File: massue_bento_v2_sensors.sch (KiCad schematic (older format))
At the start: 0 parts

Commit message: Merge branch 'master' of https://github.com/tommag/massue_bento_v2
Conflicts:
	massue_bento_v2_power.sch
	massue_bento_v2_rf.sch
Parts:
- added C?: 10nF, symbol C
- added C? (x2): 0.1uF, symbol C
- added C?: 2.2nF, symbol C
- added C?: 100nF, symbol C
- added U?: MPU9150, symbol MPU9150
- added U?: MS5607, symbol MS5607
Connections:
- new net: C?.1, U?.10 (REGOUT)
- new net: C?.2, U?.20 (CPOUT)
- new net +3.3V: C?.1, C?.1, C?.1, U?.1 (VDD), U?.13 (VDD), U?.2 (PS), U?.3 (VDD), U?.8 (VLOGIC)
- new net GND: C?.1, C?.2, C?.2, C?.2, C?.2, U?.1 (CLKIN), U?.11 (FSYNC), U?.15 (GND), U?.17 (GND), U?.18 (GND), U?.3 (GND), U?.4 (CSB), U?.5 (CSB), U?.9 (AD0)
- new net MPU9150_INT: U?.12 (INT)
- new net SCL: U?.23 (SCL), U?.8 (SCLK)
- new net SDA: U?.24 (SDA), U?.7 (SDI/SDA)
- no-connect marks 0 -> 3

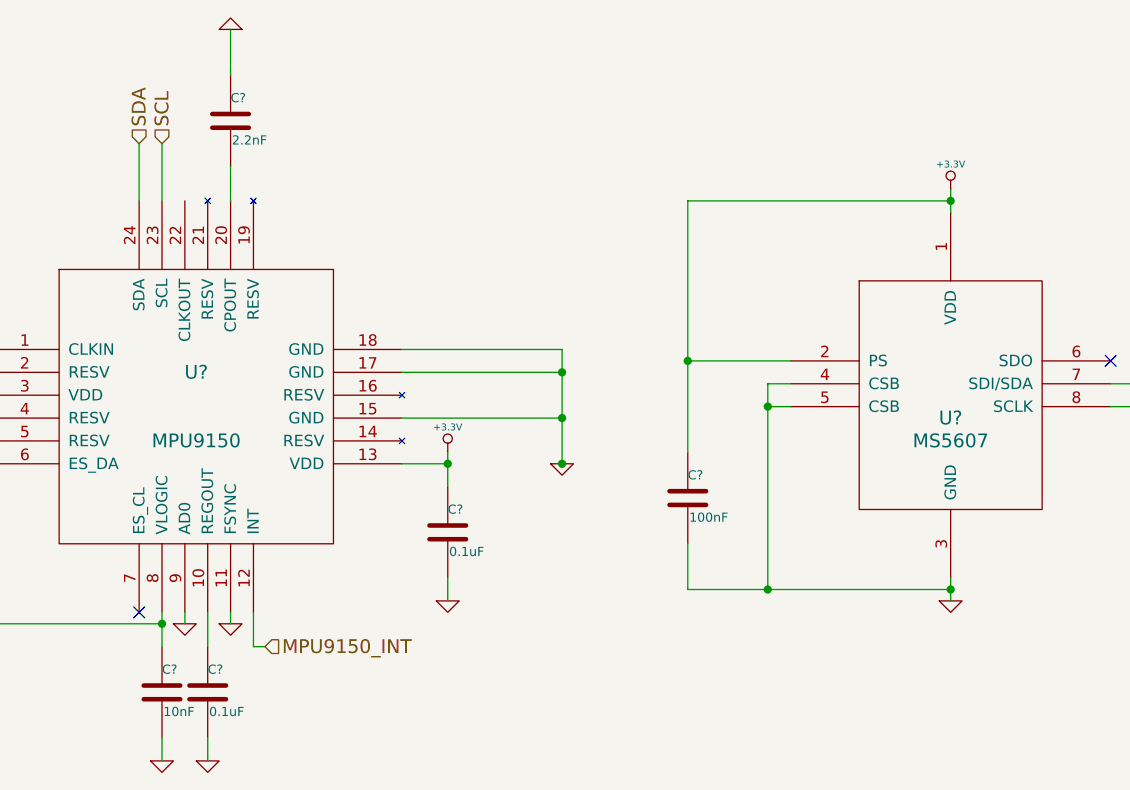
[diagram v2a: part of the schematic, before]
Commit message: Fix: global annotation, fixed bugs to satisfy ERC
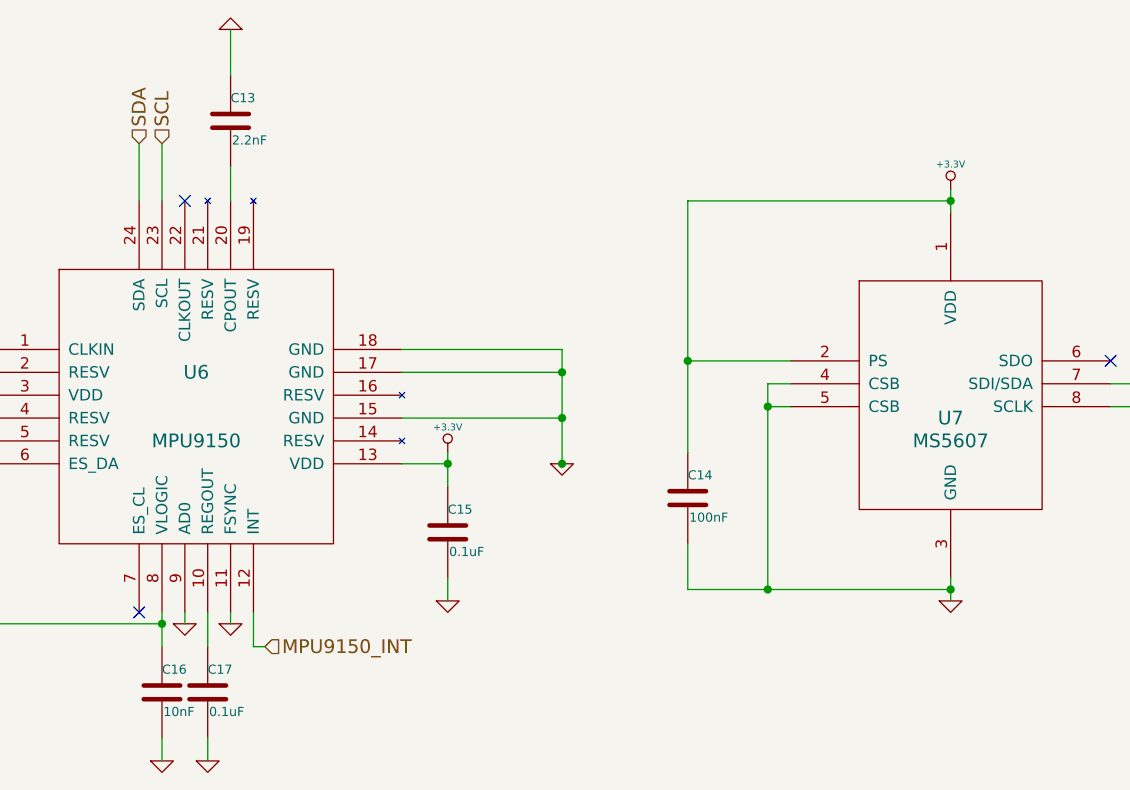
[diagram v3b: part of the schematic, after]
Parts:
- gave numbers to parts that had none: 7
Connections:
- no-connect marks 3 -> 4
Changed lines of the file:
@@
 $EndDescr
 $Comp
-L MPU9150 U?
+L MPU9150 U6
 U 1 1 53A574BD
 P 5700 4250
-F 0 "U?" H 5700 4400 60  0000 C CNN
+F 0 "U6" H 5700 4400 60  0000 C CNN
 F 1 "MPU9150" H 5700 4100 60  0000 C CNN
 F 2 "" H 5700 4250 60  0000 C CNN
@@
 SCL
 $Comp
-L GND #PWR?
+L GND #PWR057
 U 1 1 53A57668
 P 7300 4500
-F 0 "#PWR?" H 7300 4500 30  0001 C CNN
+F 0 "#PWR057" H 7300 4500 30  0001 C CNN
 F 1 "GND" H 7300 4430 30  0001 C CNN
 F 2 "" H 7300 4500 60  0000 C CNN
@@
 $EndComp
 $Comp
-L +3.3V #PWR?
+L +3.3V #PWR058
 U 1 1 53A57758
 P 6800 4450
-F 0 "#PWR?" H 6800 4410 30  0001 C CNN
+F 0 "#PWR058" H 6800 4410 30  0001 C CNN
 F 1 "+3.3V" H 6800 4560 30  0000 C CNN
 F 2 "" H 6800 4450 60  0000 C CNN
@@
 $EndComp
 $Comp
-L +3.3V #PWR?
+L +3.3V #PWR059
 U 1 1 53A57777
 P 4300 4200
-F 0 "#PWR?" H 4300 4160 30  0001 C CNN
+F 0 "#PWR059" H 4300 4160 30  0001 C CNN
 F 1 "+3.3V" H 4300 4310 30  0000 C CNN
 F 2 "" H 4300 4200 60  0000 C CNN
@@
 $EndComp
 $Comp
-L C C?
+L C C16
 U 1 1 53A57917
 P 5550 5500
-F 0 "C?" H 5550 5600 40  0000 L CNN
+F 0 "C16" H 5550 5600 40  0000 L CNN
 F 1 "10nF" H 5556 5415 40  0000 L CNN
 F 2 "" H 5588 5350 30  0000 C CNN
@@
 $EndComp
 $Comp
-L GND #PWR?
+L GND #PWR060
 U 1 1 53A57951
 P 5550 5800
-F 0 "#PWR?" H 5550 5800 30  0001 C CNN
+F 0 "#PWR060" H 5550 5800 30  0001 C CNN
 F 1 "GND" H 5550 5730 30  0001 C CNN
 F 2 "" H 5550 5800 60  0000 C CNN
@@
 $EndComp
 $Comp
-L C C?
+L C C15
 U 1 1 53A57996
 P 6800 4800
-F 0 "C?" H 6800 4900 40  0000 L CNN
+F 0 "C15" H 6800 4900 40  0000 L CNN
 F 1 "0.1uF" H 6806 4715 40  0000 L CNN
 F 2 "" H 6838 4650 30  0000 C CNN
@@
 $EndComp
 $Comp
-L GND #PWR?
+L GND #PWR061
 U 1 1 53A579C7
 P 6800 5100
-F 0 "#PWR?" H 6800 5100 30  0001 C CNN
+F 0 "#PWR061" H 6800 5100 30  0001 C CNN
 F 1 "GND" H 6800 5030 30  0001 C CNN
 F 2 "" H 6800 5100 60  0000 C CNN
@@
 $EndComp
 $Comp
-L C C?
+L C C17
 U 1 1 53A579EC
 P 5750 5500
-F 0 "C?" H 5750 5600 40  0000 L CNN
+F 0 "C17" H 5750 5600 40  0000 L CNN
 F 1 "0.1uF" H 5756 5415 40  0000 L CNN
 F 2 "" H 5788 5350 30  0000 C CNN
@@
 $EndComp
 $Comp
-L GND #PWR?
+L GND #PWR062
 U 1 1 53A57A0C
 P 5750 5800
-F 0 "#PWR?" H 5750 5800 30  0001 C CNN
+F 0 "#PWR062" H 5750 5800 30  0001 C CNN
 F 1 "GND" H 5750 5730 30  0001 C CNN
 F 2 "" H 5750 5800 60  0000 C CNN
@@
 NoConn ~ 5450 5150
 $Comp
-L GND #PWR?
+L GND #PWR063
 U 1 1 53A57AC0
 P 5650 5200
-F 0 "#PWR?" H 5650 5200 30  0001 C CNN
+F 0 "#PWR063" H 5650 5200 30  0001 C CNN
 F 1 "GND" H 5650 5130 30  0001 C CNN
 F 2 "" H 5650 5200 60  0000 C CNN
@@
 $EndComp
 $Comp
-L GND #PWR?
+L GND #PWR064
 U 1 1 53A57AE9
 P 5850 5200
-F 0 "#PWR?" H 5850 5200 30  0001 C CNN
+F 0 "#PWR064" H 5850 5200 30  0001 C CNN
 F 1 "GND" H 5850 5130 30  0001 C CNN
 F 2 "" H 5850 5200 60  0000 C CNN
@@
 MPU9150_INT
 $Comp
-L GND #PWR?
+L GND #PWR065
 U 1 1 53A57B2B
 P 4650 4050
-F 0 "#PWR?" H 4650 4050 30  0001 C CNN
+F 0 "#PWR065" H 4650 4050 30  0001 C CNN
 F 1 "GND" H 4650 3980 30  0001 C CNN
 F 2 "" H 4650 4050 60  0000 C CNN
@@
 $EndComp
 $Comp
-L C C?
+L C C13
 U 1 1 53A57B7E
 P 5850 3000
-F 0 "C?" H 5850 3100 40  0000 L CNN
+F 0 "C13" H 5850 3100 40  0000 L CNN
 F 1 "2.2nF" H 5856 2915 40  0000 L CNN
 F 2 "" H 5888 2850 30  0000 C CNN
@@
 $EndComp
 $Comp
-L GND #PWR?
+L GND #PWR066
 U 1 1 53A57BB8
 P 5850 2600
-F 0 "#PWR?" H 5850 2600 30  0001 C CNN
+F 0 "#PWR066" H 5850 2600 30  0001 C CNN
 F 1 "GND" H 5850 2530 30  0001 C CNN
 F 2 "" H 5850 2600 60  0000 C CNN
@@
 $EndComp
 $Comp
-L MS5607 U?
+L MS5607 U7
 U 1 1 53A587E2
 P 9000 4300
-F 0 "U?" H 9000 4300 60  0000 C CNN
+F 0 "U7" H 9000 4300 60  0000 C CNN
 F 1 "MS5607" H 9000 4200 60  0000 C CNN
 F 2 "" H 9000 4300 60  0000 C CNN
@@
 $EndComp
 $Comp
-L GND #PWR?
+L GND #PWR067
 U 1 1 53A587F6
 P 9000 5100
-F 0 "#PWR?" H 9000 5100 30  0001 C CNN
+F 0 "#PWR067" H 9000 5100 30  0001 C CNN
 F 1 "GND" H 9000 5030 30  0001 C CNN
 F 2 "" H 9000 5100 60  0000 C CNN
@@
 $EndComp
 $Comp
-L +3.3V #PWR?
+L +3.3V #PWR068
 U 1 1 53A58808
 P 9000 3300
-F 0 "#PWR?" H 9000 3260 30  0001 C CNN
+F 0 "#PWR068" H 9000 3260 30  0001 C CNN
 F 1 "+3.3V" H 9000 3410 30  0000 C CNN
 F 2 "" H 9000 3300 60  0000 C CNN
@@
 $EndComp
 $Comp
-L C C?
+L C C14
 U 1 1 53A58856
 P 7850 4650
-F 0 "C?" H 7850 4750 40  0000 L CNN
+F 0 "C14" H 7850 4750 40  0000 L CNN
 F 1 "100nF" H 7856 4565 40  0000 L CNN
 F 2 "" H 7888 4500 30  0000 C CNN
@@
 	9700 4250 9850 4250
 NoConn ~ 9700 4050
+NoConn ~ 5650 3350
 $EndSCHEMATC

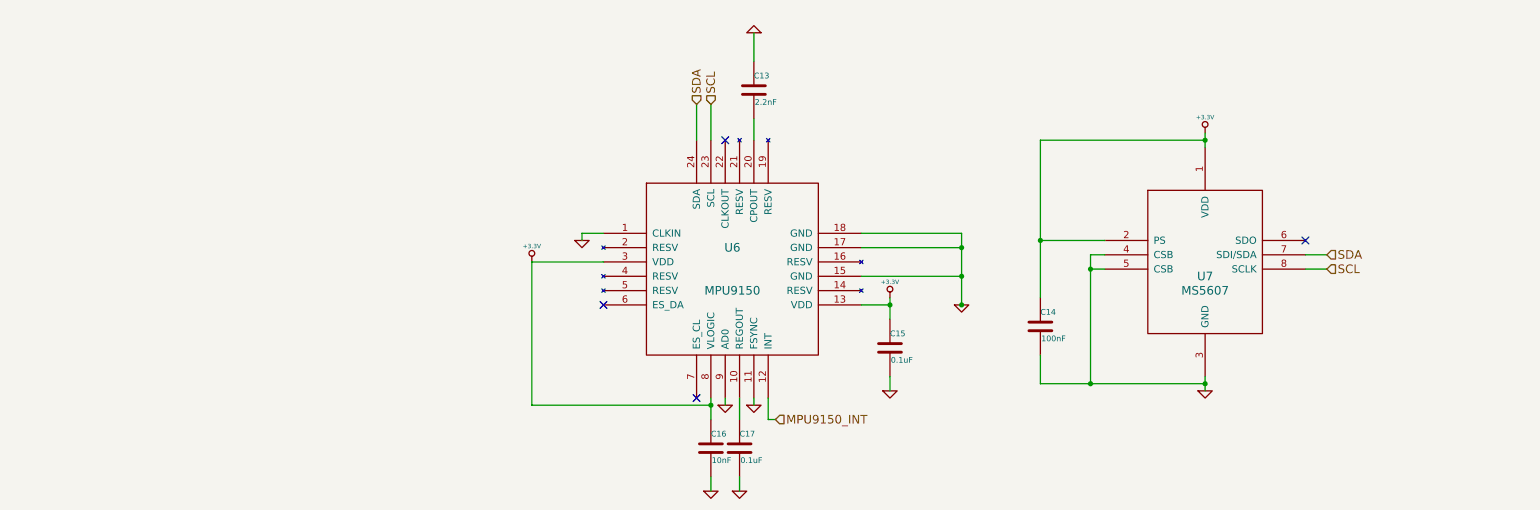
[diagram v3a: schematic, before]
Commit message: New : AT42 sensor
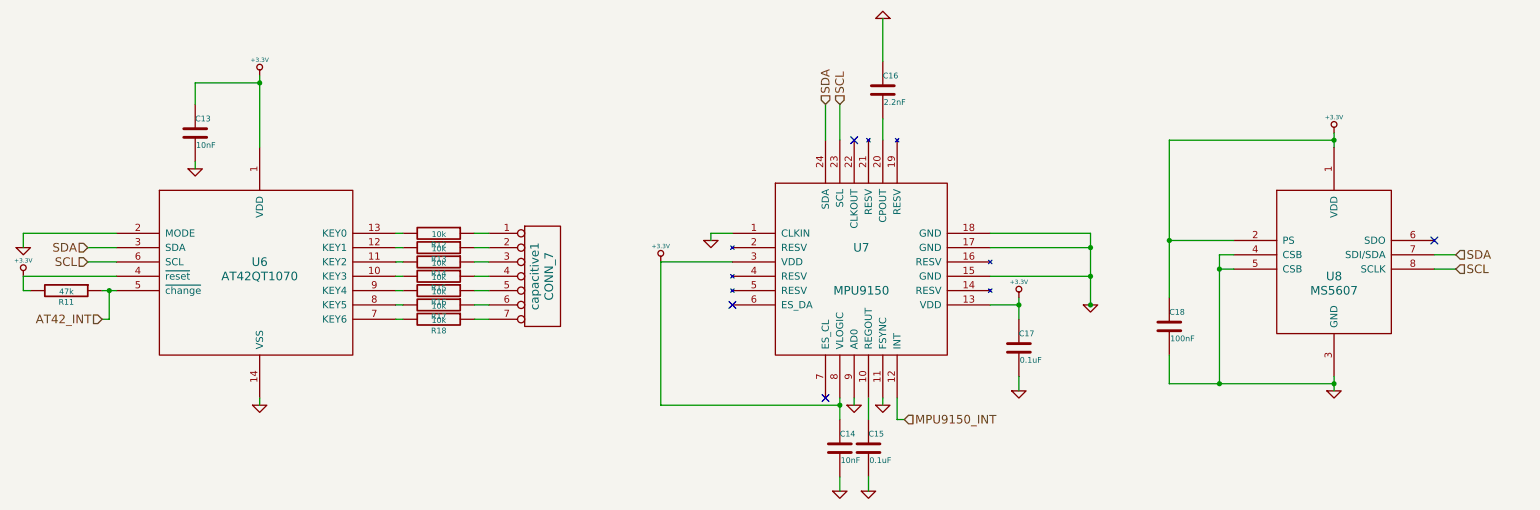
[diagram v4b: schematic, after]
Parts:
- added C13: 10nF, symbol C
- added R11: 47k, symbol R
- added R12, R13, R14, R15, R16, R17, R18: 10k, symbol R
- added U6: AT42QT1070, symbol AT42QT1070
- added capacitive1: CONN_7, symbol CONN_7
- renumbered C16 to C14, C17 to C15, C13 to C16, C15 to C17, C14 to C18, U6 to U7, U7 to U8
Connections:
- net +3.3V: now also C13.1, R11.2, U6.1 (VDD), U6.4 (~reset)
- net GND: now also C13.2, U6.14 (VSS), U6.2 (MODE)
- net SCL: now also U6.6 (SCL)
- net SDA: now also U6.3 (SDA)
- new net: R15.2, U6.10 (KEY3)
- new net: R14.2, U6.11 (KEY2)
- new net: R13.2, U6.12 (KEY1)
- new net: R12.2, U6.13 (KEY0)
- new net: R18.2, U6.7 (KEY6)
- new net: R17.2, U6.8 (KEY5)
- new net: R16.2, U6.9 (KEY4)
- new net: R12.1, capacitive1.1 (P1)
- new net: R13.1, capacitive1.2 (P2)
- new net: R14.1, capacitive1.3 (P3)
- new net: R15.1, capacitive1.4 (P4)
- new net: R16.1, capacitive1.5 (P5)
- new net: R17.1, capacitive1.6 (P6)
- new net: R18.1, capacitive1.7 (P7)
- new net AT42_INT: R11.1, U6.5 (~change)
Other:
- moved on the sheet: C14, C15, C16, C17, C18, U7, U8

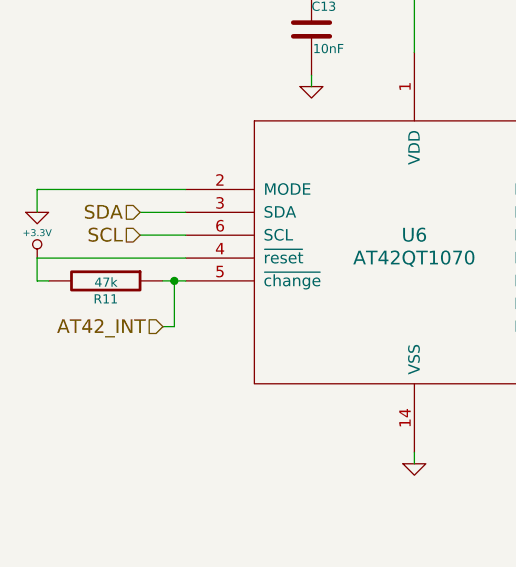
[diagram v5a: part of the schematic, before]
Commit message: Clean: remove unnecessary pull-up resistor (integrated in MCU)
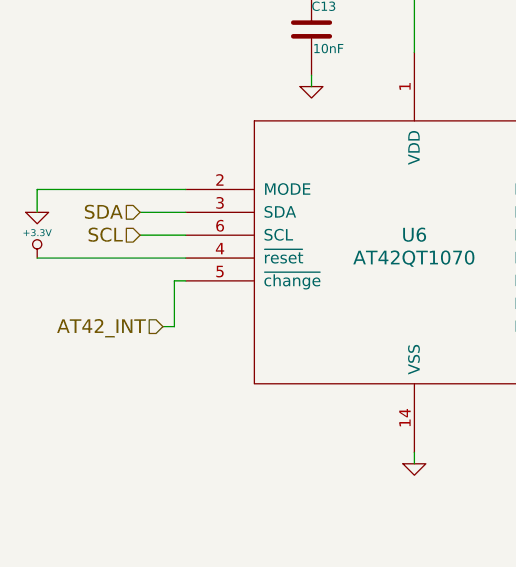
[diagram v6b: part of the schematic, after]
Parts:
- removed R11: 47k, symbol R
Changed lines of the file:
@@
 	1400 4300 750  4300
-$Comp
-L R R11
-U 1 1 53A70F8B
-P 1050 4400
-F 0 "R11" V 1130 4400 40  0000 C CNN
-F 1 "47k" V 1057 4401 40  0000 C CNN
-F 2 "" V 980 4400 30  0000 C CNN
-F 3 "" H 1050 4400 30  0000 C CNN
-	1    1050 4400
-	0    1    1    0
-$EndComp
-Wire Wire Line
-	750  4300 750  4400
 $Comp
 L C C13
@@
 AT42_INT
 Wire Wire Line
-	1300 4400 1400 4400
-Wire Wire Line
 	1300 4600 1350 4600
-Wire Wire Line
-	1350 4600 1350 4400
-Connection ~ 1350 4400
 $Comp
 L CONN_7 capacitive1
@@
 $EndComp
 Wire Wire Line
-	750  4400 800  4400
+	1350 4600 1350 4400
+Wire Wire Line
+	1350 4400 1400 4400
 $EndSCHEMATC

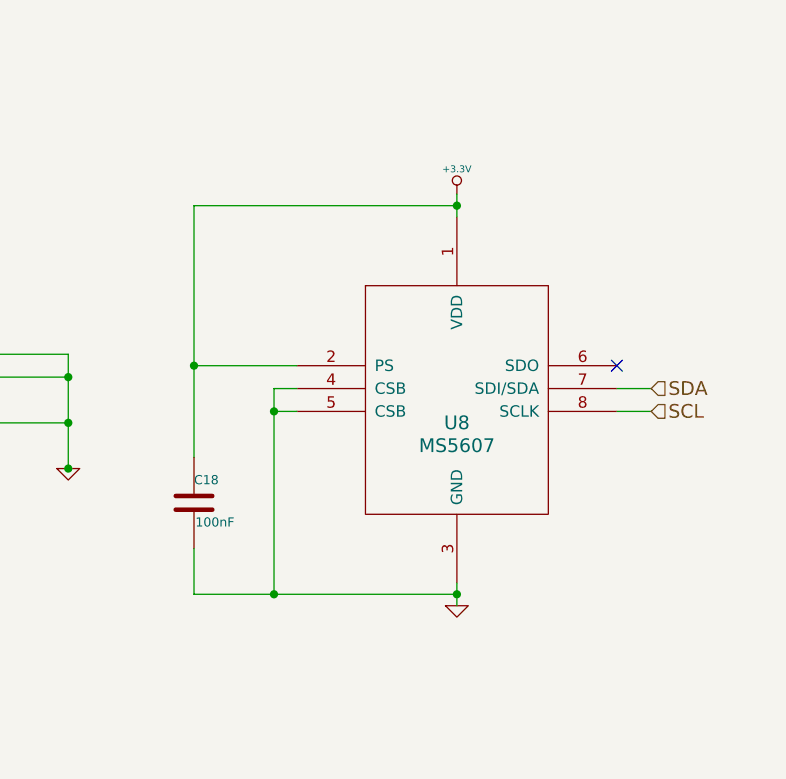
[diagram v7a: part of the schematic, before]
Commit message: Changed MS5607 altimeter for MPL3115A2
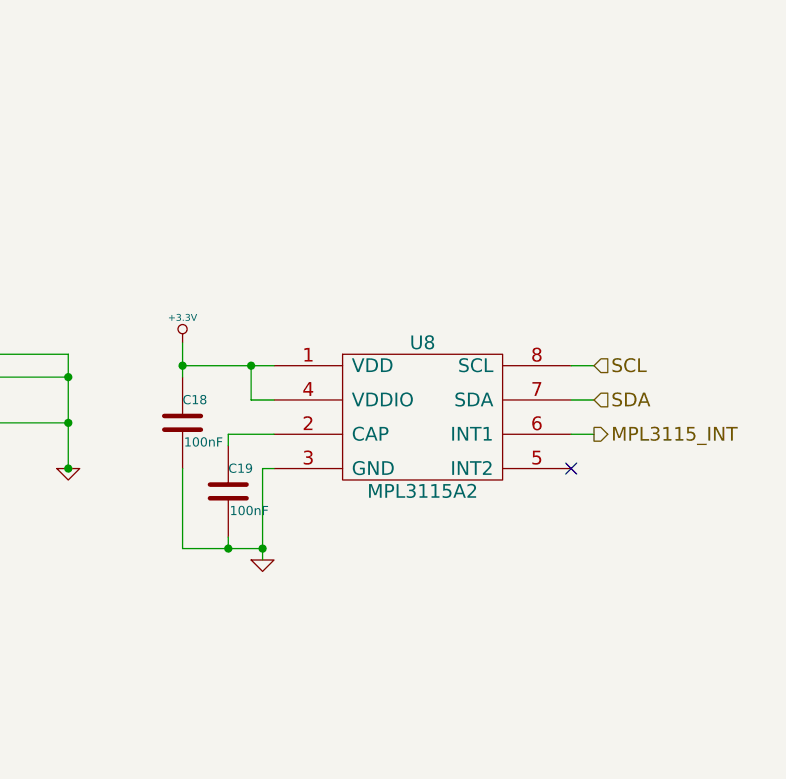
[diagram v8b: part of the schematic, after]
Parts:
- removed U8: MS5607, symbol MS5607
- added C19: 100nF, symbol C
- added U8: MPL3115A2, symbol MPL3115A2
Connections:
- net +3.3V: now also U8.1 (VDD), U8.4 (VDDIO)
- net GND: now also C19.2, U8.3 (GND)
- net SCL: now also U8.8 (SCL)
- net SDA: now also U8.7 (SDA)
- new net: C19.1, U8.2 (CAP)
- new net MPL3115_INT: U8.6 (INT1)
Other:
- moved on the sheet: C18
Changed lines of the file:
@@
-$EndComp
-$Comp
-L MS5607 U8
-U 1 1 53A587E2
-P 9900 4300
-F 0 "U8" H 9900 4300 60  0000 C CNN
-F 1 "MS5607" H 9900 4200 60  0000 C CNN
-F 2 "" H 9900 4300 60  0000 C CNN
-F 3 "" H 9900 4300 60  0000 C CNN
-	1    9900 4300
-	1    0    0    -1
 $EndComp
 $Comp
 L GND #PWR050
 U 1 1 53A587F6
-P 9900 5100
-F 0 "#PWR050" H 9900 5100 30  0001 C CNN
-F 1 "GND" H 9900 5030 30  0001 C CNN
-F 2 "" H 9900 5100 60  0000 C CNN
-F 3 "" H 9900 5100 60  0000 C CNN
-	1    9900 5100
+P 9050 4900
+F 0 "#PWR050" H 9050 4900 30  0001 C CNN
+F 1 "GND" H 9050 4830 30  0001 C CNN
+F 2 "" H 9050 4900 60  0000 C CNN
+F 3 "" H 9050 4900 60  0000 C CNN
+	1    9050 4900
 	1    0    0    -1
 $EndComp
@@
 L +3.3V #PWR051
 U 1 1 53A58808
-P 9900 3300
-F 0 "#PWR051" H 9900 3260 30  0001 C CNN
-F 1 "+3.3V" H 9900 3410 30  0000 C CNN
-F 2 "" H 9900 3300 60  0000 C CNN
-F 3 "" H 9900 3300 60  0000 C CNN
-	1    9900 3300
+P 8700 3950
+F 0 "#PWR051" H 8700 3910 30  0001 C CNN
+F 1 "+3.3V" H 8700 4060 30  0000 C CNN
+F 2 "" H 8700 3950 60  0000 C CNN
+F 3 "" H 8700 3950 60  0000 C CNN
+	1    8700 3950
 	1    0    0    -1
 $EndComp
@@
 L C C18
 U 1 1 53A58856
-P 8750 4650
-F 0 "C18" H 8750 4750 40  0000 L CNN
-F 1 "100nF" H 8756 4565 40  0000 L CNN
-F 2 "" H 8788 4500 30  0000 C CNN
-F 3 "" H 8750 4650 60  0000 C CNN
-	1    8750 4650
-	1    0    0    -1
-$EndComp
-Connection ~ 9100 4250
-Wire Wire Line
-	9200 4150 9100 4150
-Connection ~ 9100 5050
-Wire Wire Line
-	9100 4150 9100 5050
-Wire Wire Line
-	9200 4250 9100 4250
-Connection ~ 8750 4050
-Wire Wire Line
-	9200 4050 8750 4050
-Wire Wire Line
-	8750 3350 9900 3350
-Wire Wire Line
-	8750 3350 8750 4450
-Connection ~ 9900 5050
-Wire Wire Line
-	8750 5050 9900 5050
-Wire Wire Line
-	8750 4850 8750 5050
-Connection ~ 9900 3350
-Wire Wire Line
-	9900 5000 9900 5100
-Wire Wire Line
-	9900 3300 9900 3400
+P 8700 4300
+F 0 "C18" H 8700 4400 40  0000 L CNN
+F 1 "100nF" H 8706 4215 40  0000 L CNN
+F 2 "" H 8738 4150 30  0000 C CNN
+F 3 "" H 8700 4300 60  0000 C CNN
+	1    8700 4300
+	1    0    0    -1
+$EndComp
 Connection ~ 6450 5200
 Wire Wire Line
@@
 Wire Wire Line
 	7500 4000 8200 4000
-Text HLabel 10750 4150 2    60   Input ~ 0
+Text HLabel 10500 4200 2    60   Input ~ 0
 SDA
-Text HLabel 10750 4250 2    60   Input ~ 0
+Text HLabel 10500 4050 2    60   Input ~ 0
 SCL
-Wire Wire Line
-	10600 4150 10750 4150
-Wire Wire Line
-	10600 4250 10750 4250
-NoConn ~ 10600 4050
 NoConn ~ 6550 3350
 $Comp
@@
 Wire Wire Line
 	1350 4400 1400 4400
+$Comp
+L MPL3115A2 U8
+U 1 1 53B4FCAB
+P 9750 4300
+F 0 "U8" H 9750 4650 60  0000 C CNN
+F 1 "MPL3115A2" H 9750 4000 60  0000 C CNN
+F 2 "" H 9750 4300 60  0000 C CNN
+F 3 "" H 9750 4300 60  0000 C CNN
+	1    9750 4300
+	1    0    0    -1
+$EndComp
+$Comp
+L C C19
+U 1 1 53B4FE20
+P 8900 4600
+F 0 "C19" H 8900 4700 40  0000 L CNN
+F 1 "100nF" H 8906 4515 40  0000 L CNN
+F 2 "" H 8938 4450 30  0000 C CNN
+F 3 "" H 8900 4600 60  0000 C CNN
+	1    8900 4600
+	1    0    0    -1
+$EndComp
+Wire Wire Line
+	8700 3950 8700 4100
+Wire Wire Line
+	8700 4050 9100 4050
+Wire Wire Line
+	9100 4200 9000 4200
+Wire Wire Line
+	9000 4200 9000 4050
+Connection ~ 9000 4050
+Connection ~ 8700 4050
+Wire Wire Line
+	8900 4350 9100 4350
+Wire Wire Line
+	9100 4500 9050 4500
+Wire Wire Line
+	9050 4500 9050 4900
+Wire Wire Line
+	8900 4800 8900 4850
+Connection ~ 9050 4850
+Wire Wire Line
+	8700 4500 8700 4850
+Wire Wire Line
+	8900 4400 8900 4350
+Wire Wire Line
+	8700 4850 9050 4850
+Connection ~ 8900 4850
+Wire Wire Line
+	10400 4200 10500 4200
+Wire Wire Line
+	10400 4050 10500 4050
+NoConn ~ 10400 4500
+Text HLabel 10500 4350 2    60   Output ~ 0
+MPL3115_INT
+Wire Wire Line
+	10400 4350 10500 4350
 $EndSCHEMATC
